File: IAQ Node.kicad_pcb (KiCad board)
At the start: 2 copper layers, 58 x 39 mm, 22 parts, among them J1 Conn_01x02_Male, J2 Conn_01x06_Male, J3 Conn_01x07_Male, U1 ATSAML21E18B-AUT, U2 BME680, U3 CCS811

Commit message: Alpha release of PCB
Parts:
- removed REF** (x4): MountingHole_3.2mm_M3, MountingHole:MountingHole_3.2mm_M3
- added C10: 100n, Capacitor_SMD:C_0402_1005Metric, F.Cu at (168.2, 100.8)
- added C11: 100n, Capacitor_SMD:C_0402_1005Metric, F.Cu at (168.2, 108.5)
- added C8: 100n, Capacitor_SMD:C_0402_1005Metric, F.Cu at (168.2, 110.5)
- added C9: 1u, Capacitor_SMD:C_0402_1005Metric, F.Cu at (170.8, 107.0)
- added D1: LED_Small, Resistor_SMD:R_0603_1608Metric, F.Cu at (139.5, 93.0)
- added D2: LED_Small, Resistor_SMD:R_0603_1608Metric, F.Cu at (149.5, 93.0)
- added D3: LED_Small, Resistor_SMD:R_0603_1608Metric, F.Cu at (159.5, 93.0)
- added H1: MountingHole_Pad, MountingHole:MountingHole_3.2mm_M3_Pad, F.Cu at (128.0, 93.5)
- added H2: MountingHole_Pad, MountingHole:MountingHole_3.2mm_M3_Pad, F.Cu at (128.0, 116.5)
- added H3: MountingHole_Pad, MountingHole:MountingHole_3.2mm_M3_Pad, F.Cu at (170.0, 116.5)
- added H4: MountingHole_Pad, MountingHole:MountingHole_3.2mm_M3_Pad, F.Cu at (170.0, 93.5)
- added L1: 10uH, Inductor_SMD:L_0805_2012Metric, F.Cu at (142.0, 103.5)
- added R5: 2k2, Resistor_SMD:R_0402_1005Metric, F.Cu at (165.8, 100.8)
- added R6: 4k7, Resistor_SMD:R_0402_1005Metric, F.Cu at (168.2, 103.0)
- added U4: OPT3001, Package_DFN_QFN:DFN-6-1EP_2x2mm_P0.65mm_EP1x1.6mm, F.Cu at (170.8, 100.8)
- J1: value Conn_01x02_Male -> JST S2B-ZR-SMA4-TF
- J2: value Conn_01x06_Male -> JST S7B-ZR-SMA4-TF; footprint Connector_JST:JST_ZE_SM06B-ZESS-TBT_1x06-1MP_P1.50mm_Horizontal -> Connector_JST:JST_ZE_SM07B-ZESS-TBT_1x07-1MP_P1.50mm_Horizontal
- J3: value Conn_01x07_Male -> JST S7B-ZR-SMA4-TF
- R3: value 2k2 -> R_Small
- moved FB1 38.1 mm to (155.5, 108.2)
- moved C1 37.9 mm to (155.5, 106.2), turned to 90 degrees
- moved J2 37.7 mm to (140.2, 114.8), turned to 0 degrees
- moved C2 36.1 mm to (154.5, 106.2), turned to 90 degrees
- moved R4 35.4 mm to (166.8, 100.8), turned to 90 degrees
- moved J3 34.6 mm to (157.5, 114.8)
- moved U2 30.9 mm to (170.8, 109.5)
- moved R3 30.8 mm to (157.0, 93.0), turned to 0 degrees
- moved U3 27.4 mm to (170.8, 104.2)
- moved J1 27.4 mm to (129.8, 102.2)
- moved U1 26.1 mm to (148.5, 103.8), turned to 90 degrees
- moved R2 23.1 mm to (147.0, 93.0), turned to 0 degrees
- moved C7 19.5 mm to (142.0, 106.8), turned to 180 degrees
- moved C6 18.6 mm to (142.0, 105.8), turned to 180 degrees
- moved C4 17.2 mm to (142.0, 101.2), turned to 180 degrees
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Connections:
- net Net-(C1-Pad1) renamed /VDDA
- net Net-(C3-Pad1) renamed /VDDCORE
- net Net-(C5-Pad1) renamed /VSW
- J2 pad 3: /CLK -> /SWCLK
- J2 pad 4: /CS -> /SWDIO
- J2 pad 5: /SDI -> /RESET
- J2 pad 6: /D_C -> /UART_RX
- J3 pad 1: /SWDIO -> VDD
- J3 pad 2: /SWCLK -> GND
- J3 pad 3: /RESET -> /CLK
- J3 pad 4: GND -> /CS
- J3 pad 5: VDD -> /SDI
- J3 pad 6: /UART_RX -> /D_C
- J3 pad 7: /UART_TX -> /BUSY
- R1 pad 2: /VBAT_SENSE -> Net-(D1-Pad2)
- R2 pad 1: /VBAT_SENSE -> /LED1
- R2 pad 2: GND -> Net-(D2-Pad2)
- R3 pad 1: VDD -> /LED2
- R3 pad 2: /I2C_SDA -> Net-(D3-Pad2)
- R4 pad 2: /I2C_SCL -> /I2C_SDA
- U1 pad 1: Net-(U1-Pad1) -> /UART_RX
- U1 pad 11: Net-(U1-Pad11) -> /CLK
- U1 pad 12: Net-(U1-Pad12) -> /CS
- U1 pad 13: Net-(U1-Pad13) -> /SDI
- U1 pad 14: Net-(U1-Pad14) -> /D_C
- U1 pad 15: Net-(U1-Pad15) -> /BUSY
- U1 pad 16: Net-(U1-Pad16) -> /CSS811_INT
- U1 pad 17: /UART_TX -> /I2C_SDA
- U1 pad 18: /UART_RX -> /I2C_SCL
- U1 pad 19: Net-(U1-Pad19) -> /OPT3001_INT
- U1 pad 2: Net-(U1-Pad2) -> /UART_TX
- U1 pad 20: Net-(U1-Pad20) -> /CCS81_WAKE
- U1 pad 21: /I2C_SDA -> /LED2
- U1 pad 22: /I2C_SCL -> /LED1
- U1 pad 23: Net-(U1-Pad23) -> (no net)
- U1 pad 24: Net-(U1-Pad24) -> (no net)
- U1 pad 25: Net-(U1-Pad25) -> (no net)
- U1 pad 3: Net-(U1-Pad3) -> (no net)
- U1 pad 4: Net-(U1-Pad4) -> (no net)
- U1 pad 5: Net-(U1-Pad5) -> (no net)
- U1 pad 6: Net-(U1-Pad6) -> (no net)
- U1 pad 7: Net-(U1-Pad7) -> (no net)
- U1 pad 8: Net-(U1-Pad8) -> (no net)
- U2 pad 1: Net-(U2-Pad1) -> GND
- U2 pad 2: Net-(U2-Pad2) -> VDD
- U2 pad 3: Net-(U2-Pad3) -> /I2C_SDA
- U2 pad 4: Net-(U2-Pad4) -> /I2C_SCL
- U2 pad 5: Net-(U2-Pad5) -> GND
- U2 pad 6: Net-(U2-Pad6) -> VDD
- U2 pad 7: Net-(U2-Pad7) -> GND
- U2 pad 8: Net-(U2-Pad8) -> VDD
- U3 pad 1: Net-(U3-Pad1) -> GND
- U3 pad 10: Net-(U3-Pad10) -> /I2C_SCL
- U3 pad 11: Net-(U3-Pad11) -> GND
- U3 pad 3: Net-(U3-Pad3) -> /CSS811_INT
- U3 pad 5: Net-(U3-Pad5) -> Net-(U3-Pad4)
- U3 pad 6: Net-(U3-Pad6) -> VDD
- U3 pad 7: Net-(U3-Pad7) -> /CCS81_WAKE
- U3 pad 8: Net-(U3-Pad8) -> (no net)
- U3 pad 9: Net-(U3-Pad9) -> /I2C_SDA
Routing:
- net VDD: track 0.00 -> 106.9 mm, vias 0 -> 2
- net GND: track 0.00 -> 45.4 mm, vias 0 -> 14
- net /I2C_SCL: track 0.00 -> 40.6 mm, vias 0 -> 4
- net /I2C_SDA: track 0.00 -> 40.4 mm, vias 0 -> 3
- net /CCS81_WAKE: track 0.00 -> 34.7 mm
- net /OPT3001_INT: track 0.00 -> 27.8 mm
- net /CSS811_INT: track 0.00 -> 18.3 mm
- net /BUSY: track 0.00 -> 16.2 mm
- net /D_C: track 0.00 -> 14.9 mm
- net /SDI: track 0.00 -> 13.6 mm
- net /RESET: track 0.00 -> 13.3 mm, vias 0 -> 2
- net /CS: track 0.00 -> 13.1 mm
- net /CLK: track 0.00 -> 12.6 mm
- net /LED2: track 0.00 -> 11.8 mm
- net /SWCLK: track 0.00 -> 10.2 mm
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- added copper zone on B.Cu, net GND
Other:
- board size 58 x 39 mm -> 50 x 31 mm
- net class Power added: clearance 0.2, trace_width 0.4, via_dia 0.8, via_drill 0.4
- board text added: "ACT"
- board text added: "Farving Labs"
- board text added: "IAQ Node"
- board text added: "PWR"
- board text added: "Rev 1.0"
- board text added: "WAKE"

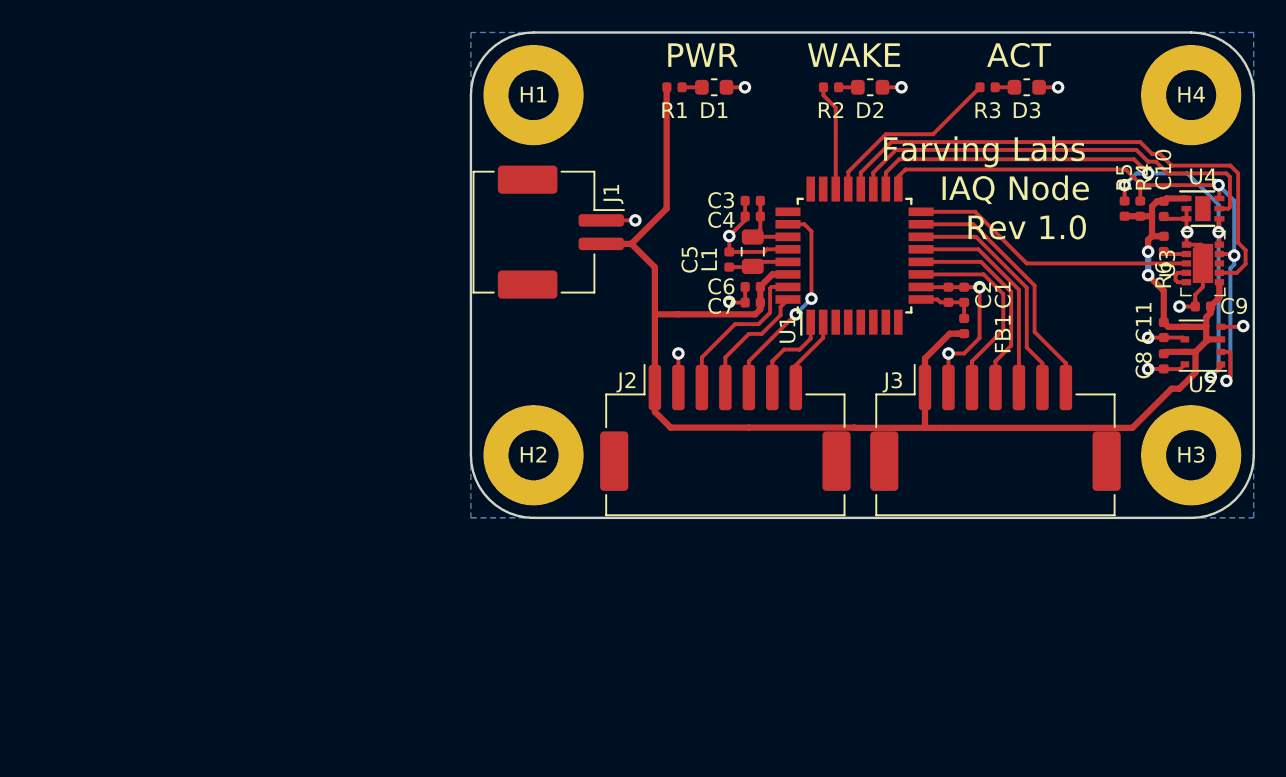
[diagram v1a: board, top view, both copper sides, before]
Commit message: Changed connector
Removed JST 8way
Added Tag-connect SWD connector
Added JST 3way for UART
Major layout changes
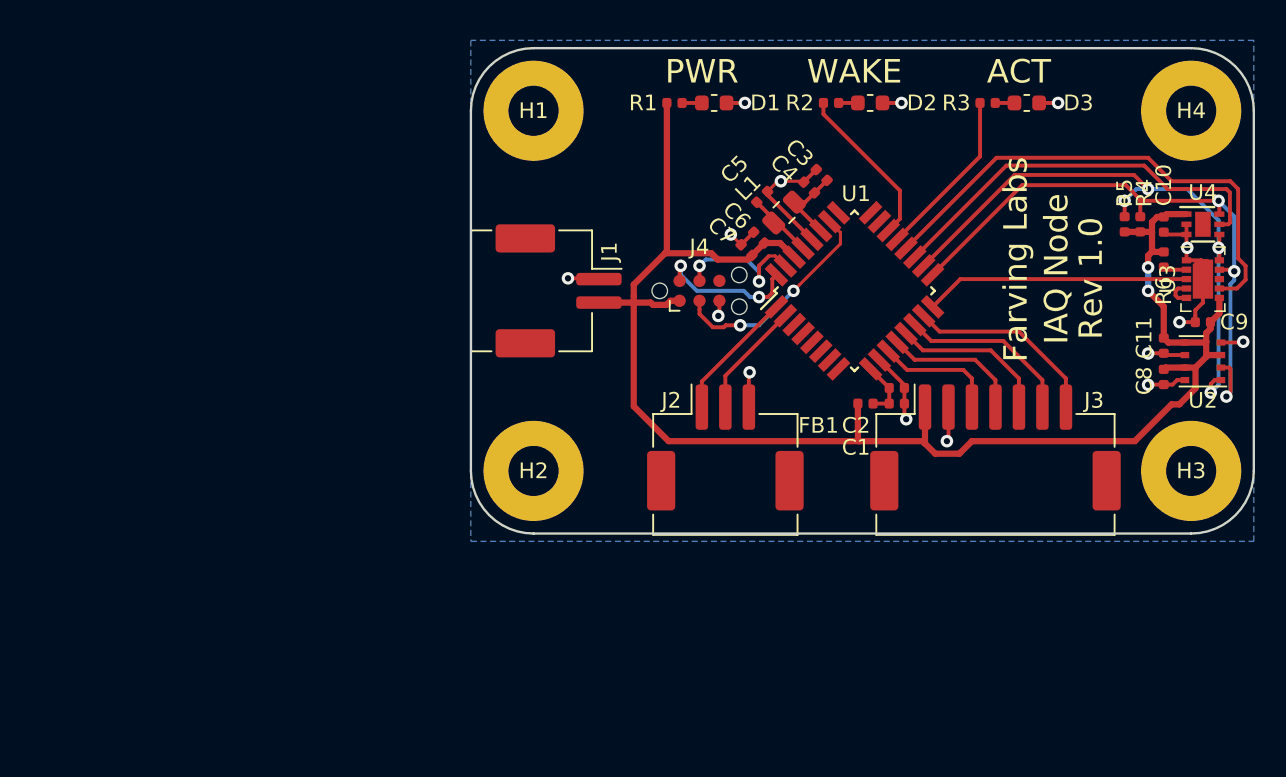
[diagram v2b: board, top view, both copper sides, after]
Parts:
- added J4: TC2030-CTX-NL, Connector:Tag-Connect_TC2030-IDC-NL_2x03_P1.27mm_Vertical, F.Cu at (138.6, 106.0)
- J2: value JST S7B-ZR-SMA4-TF -> JST S3B-ZR-SMA4-TF; footprint Connector_JST:JST_ZE_SM07B-ZESS-TBT_1x07-1MP_P1.50mm_Horizontal -> Connector_JST:JST_ZE_SM03B-ZESS-TBT_1x03-1MP_P1.50mm_Horizontal
- moved C1 8.17 mm to (151.2, 113.2), turned to 0 degrees
- moved FB1 8.01 mm to (149.2, 113.2), turned to 180 degrees
- moved C2 6.80 mm to (151.2, 112.2), turned to 0 degrees
- moved C3 4.70 mm to (146.4, 98.6), turned to 135 degrees
- moved C5 4.52 mm to (142.6, 100.0), turned to 45 degrees
- moved C4 4.05 mm to (145.6, 99.4), turned to 135 degrees
- moved J1 3.75 mm to (129.6, 106.0)
- moved C7 3.37 mm to (141.6, 103.4), turned to 135 degrees
- moved L1 3.20 mm to (144.0, 101.0), turned to 225 degrees
- moved C6 3.18 mm to (142.4, 102.6), turned to 135 degrees
- moved U1 2.25 mm to (148.5, 106.0), turned to 45 degrees
- moved J2 1.25 mm to (140.2, 116.0)
- moved J3 1.25 mm to (157.5, 116.0)
- moved C10 1.00 mm to (168.2, 101.8)
- moved C11 1.00 mm to (168.2, 109.5)
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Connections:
- J2 pad 1: VDD -> /UART_RX
- J2 pad 2: GND -> /UART_TX
- J2 pad 3: /SWCLK -> GND
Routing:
- net GND: track 45.4 -> 40.6 mm, vias 14 -> 15
- net /CLK: track 12.6 -> 7.89 mm
- net /CS: track 13.1 -> 9.00 mm
- net /LED1: track 6.83 -> 10.5 mm
- net /BUSY: track 16.2 -> 12.6 mm
- net /D_C: track 14.9 -> 11.3 mm
- net /SDI: track 13.6 -> 10.2 mm
- net /UART_RX: track 5.78 -> 8.37 mm
- net /UART_TX: track 4.90 -> 7.42 mm
- net /CCS81_WAKE: track 34.7 -> 32.3 mm
- net VDD: track 106.9 -> 104.9 mm
- net /OPT3001_INT: track 27.8 -> 25.9 mm
- net /SWDIO: track 7.77 -> 9.37 mm, vias 0 -> 2
- net /CSS811_INT: track 18.3 -> 17.0 mm
- net /I2C_SCL: track 40.6 -> 39.5 mm
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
